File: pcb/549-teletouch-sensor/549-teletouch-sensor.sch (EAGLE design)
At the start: 87 parts, among them J1 RASPBERRYPI-40-PIN-GPIO_PTH, J2 RASPBERRYPI-40-PIN-GPIO_PTH

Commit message: updated sensor pcb
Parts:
- removed H1, H2, H3, H4: STAND-OFF, SparkFun-Hardware:STAND-OFF
- removed J2: RASPBERRYPI-40-PIN-GPIO_PTH, SparkFun-Connectors:RASPBERRYPI-40-PIN-GPIO_PTH
- added IC1, IC2: MCP23017SP, adafruit:MCP23017SP
- added SENSOR_ENDS1, SENSOR_ENDS2: CONN_20X2, SparkFun-Connectors:CONN_20X2
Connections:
- removed net GP41: J1.GP26
- removed net GP42: J1.GP4
- removed net GP43: J1.GP17
- removed net GP44: J1.GP18#
- removed net GP45: J1.GP22
- removed net GP46: J1.GP23
- removed net GP47: J1.GP24
- removed net GP48: J1.GP25
- removed net GP49: J1.GP27
- removed net N$11: R10.2
- removed net N$12: R1.2
- removed net N$13: R2.2
- removed net N$14: R3.2
- removed net N$15: R4.2
- removed net N$16: R5.2
- removed net N$17: R6.2
- removed net N$18: R7.2
- removed net N$19: R8.2
- removed net N$20: R9.2
- removed net N$31: R20.2
- removed net N$32: R11.2
- removed net N$33: R12.2
- removed net N$34: R13.2
- removed net N$35: R14.2
- removed net N$36: R15.2
- removed net N$37: R16.2
- removed net N$38: R17.2
- removed net N$39: R18.2
- removed net N$40: R19.2
- removed net N$51: R30.2
- removed net N$52: R21.2
- removed net N$53: R22.2
- removed net N$54: R23.2
- removed net N$55: R24.2
- removed net N$56: R25.2
- removed net N$57: R26.2
- removed net N$58: R27.2
- removed net N$59: R28.2
- removed net N$60: R29.2
- removed net N$71: R40.2
- removed net N$72: R31.2
- removed net N$73: R32.2
- removed net N$74: R33.2
- removed net N$75: R34.2
- removed net N$76: R35.2
- removed net N$77: R36.2
- removed net N$78: R37.2
- removed net N$79: R38.2
- removed net N$80: R39.2
- new net S1: R10.2, SENSOR_ENDS1.1
- new net S10: R9.2, SENSOR_ENDS1.19
- new net S11: R20.2, SENSOR_ENDS1.21
- new net S12: R11.2, SENSOR_ENDS1.23
- new net S13: R12.2, SENSOR_ENDS1.25
- new net S14: R13.2, SENSOR_ENDS1.27
- new net S15: R14.2, SENSOR_ENDS1.29
- new net S16: R15.2, SENSOR_ENDS1.31
- new net S17: R16.2, SENSOR_ENDS1.33
- new net S18: R17.2, SENSOR_ENDS1.35
- new net S19: R18.2, SENSOR_ENDS1.37
- new net S2: R1.2, SENSOR_ENDS1.3
- new net S20: R19.2, SENSOR_ENDS1.39
- new net S21: R30.2, SENSOR_ENDS1.2
- new net S22: R21.2, SENSOR_ENDS1.4
- new net S23: R22.2, SENSOR_ENDS1.6
- new net S24: R23.2, SENSOR_ENDS1.8
- new net S25: R24.2, SENSOR_ENDS1.10
- new net S26: R25.2, SENSOR_ENDS1.12
- new net S27: R26.2, SENSOR_ENDS1.14
- new net S28: R27.2, SENSOR_ENDS1.16
- new net S29: R28.2, SENSOR_ENDS1.18
- new net S3: R2.2, SENSOR_ENDS1.5
- new net S30: R29.2, SENSOR_ENDS1.20
- new net S31: R40.2, SENSOR_ENDS1.22
- new net S32: R31.2, SENSOR_ENDS1.24
- new net S33: R32.2, SENSOR_ENDS1.26
- new net S34: R33.2, SENSOR_ENDS1.28
- new net S35: R34.2, SENSOR_ENDS1.30
- new net S36: R35.2, SENSOR_ENDS1.32
- new net S37: R36.2, SENSOR_ENDS1.34
- new net S38: R37.2, SENSOR_ENDS1.36
- new net S39: R38.2, SENSOR_ENDS1.38
- new net S4: R3.2, SENSOR_ENDS1.7
- new net S40: R39.2, SENSOR_ENDS1.40
- new net S5: R4.2, SENSOR_ENDS1.9
- new net S6: R5.2, SENSOR_ENDS1.11
- new net S7: R6.2, SENSOR_ENDS1.13
- new net S8: R7.2, SENSOR_ENDS1.15
- new net S9: R8.2, SENSOR_ENDS1.17
- net GND: now also IC1.A0, IC1.A1, IC1.A2, IC1.VSS, IC2.A1, IC2.A2, IC2.VSS
- net GP1: now also IC2.GPA0, SENSOR_ENDS2.1; no longer J2.TXO
- net GP10: now also IC2.GPB1, SENSOR_ENDS2.19; no longer J2.GP18#
- net GP11: now also IC2.GPB2, SENSOR_ENDS2.21; no longer J2.GP22
- net GP12: now also IC2.GPB3, SENSOR_ENDS2.23; no longer J2.GP23
- net GP13: now also IC2.GPB4, SENSOR_ENDS2.25; no longer J2.GP24
- net GP14: now also IC2.GPB5, SENSOR_ENDS2.27; no longer J2.GP25
- net GP15: now also IC2.GPB6, SENSOR_ENDS2.29; no longer J2.GP27
- net GP16: now also IC2.GPB7, SENSOR_ENDS2.31; no longer J2.ID_SD
- net GP17: now also IC1.GPA0, SENSOR_ENDS2.33; no longer J2.ID_SC
- net GP18: now also IC1.GPA1, SENSOR_ENDS2.35; no longer J2.5V@2
- net GP19: now also IC1.GPA2, SENSOR_ENDS2.37; no longer J2.5V@4
- net GP2: now also IC2.GPA1, SENSOR_ENDS2.3; no longer J2.RXI
- net GP20: now also IC1.GPA3, SENSOR_ENDS2.39; no longer J2.3.3V@1
- net GP21: now also IC1.GPA4, SENSOR_ENDS2.2; no longer J2.3.3V@17
- net GP22: now also IC1.GPA5, SENSOR_ENDS2.4; no longer J2.GP5
- net GP23: now also IC1.GPA6, SENSOR_ENDS2.6; no longer J2.GP6
- net GP24: now also IC1.GPA7, SENSOR_ENDS2.8; no longer J2.GP12
- net GP25: now also IC1.GPB0, SENSOR_ENDS2.10; no longer J2.GP13
- net GP26: now also IC1.GPB1, SENSOR_ENDS2.12; no longer J2.GP16
- net GP27: now also IC1.GPB2, SENSOR_ENDS2.14; no longer J2.GP19
- net GP28: now also IC1.GPB3, SENSOR_ENDS2.16; no longer J2.GP20
- net GP29: now also IC1.GPB4, SENSOR_ENDS2.18; no longer J2.GP21
- net GP3: now also IC2.GPA2, SENSOR_ENDS2.5; no longer J2.SCLK
- net GP30: now also IC1.GPB5, SENSOR_ENDS2.20; no longer J2.GP26
- net GP31: now also IC1.GPB6, SENSOR_ENDS2.22; no longer J2.GND@6
- net GP32: now also IC1.GPB7, SENSOR_ENDS2.24; no longer J2.GND@9
- net GP33: now also SENSOR_ENDS2.26; no longer J2.GND@14
- net GP34: now also SENSOR_ENDS2.28; no longer J2.GND@20
- net GP35: now also SENSOR_ENDS2.30; no longer J2.GND@25
- net GP36: now also SENSOR_ENDS2.32; no longer J2.GND@30
- net GP37: now also SENSOR_ENDS2.34; no longer J2.GND@34
- net GP38: now also SENSOR_ENDS2.36; no longer J2.GND@39
- net GP39: now also SENSOR_ENDS2.38; no longer J2.SDA
- net GP4: now also IC2.GPA3, SENSOR_ENDS2.7; no longer J2.MISO
- net GP40: now also SENSOR_ENDS2.40; no longer J2.SCL
- net GP5: now also IC2.GPA4, SENSOR_ENDS2.9; no longer J2.MOSI
- net GP6: now also IC2.GPA5, SENSOR_ENDS2.11; no longer J2.CE0
- net GP7: now also IC2.GPA6, SENSOR_ENDS2.13; no longer J2.CE1
- net GP8: now also IC2.GPA7, SENSOR_ENDS2.15; no longer J2.GP4
- net GP9: now also IC2.GPB0, SENSOR_ENDS2.17; no longer J2.GP17
- net SCL: now also IC1.SCL, IC2.SCL
- net SDA: now also IC1.SDA, IC2.SDA
- net VDD: now also IC1.!RESET, IC1.VDD, IC2.!RESET, IC2.A0, IC2.VDD
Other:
- moved on the sheet: C1, C10, C11, C12, C13, C14, C15, C16, C17, C18, C19, C2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

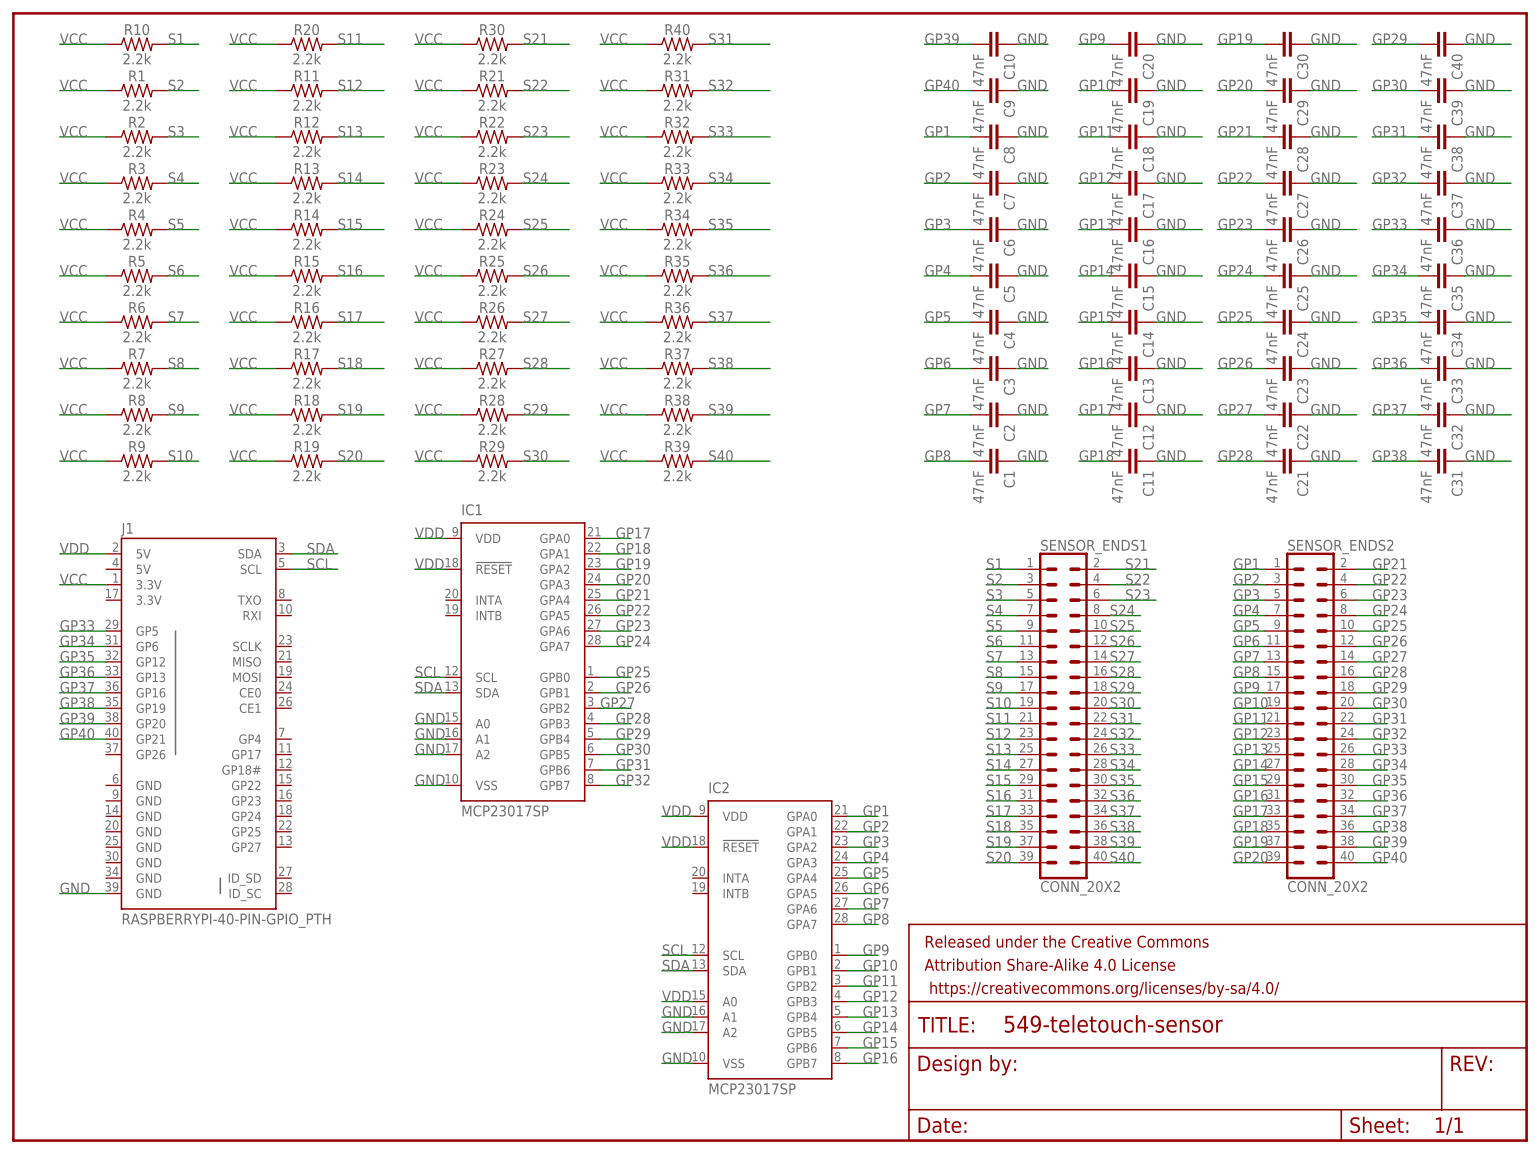
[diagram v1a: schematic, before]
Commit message: updated to half the amount of sensors
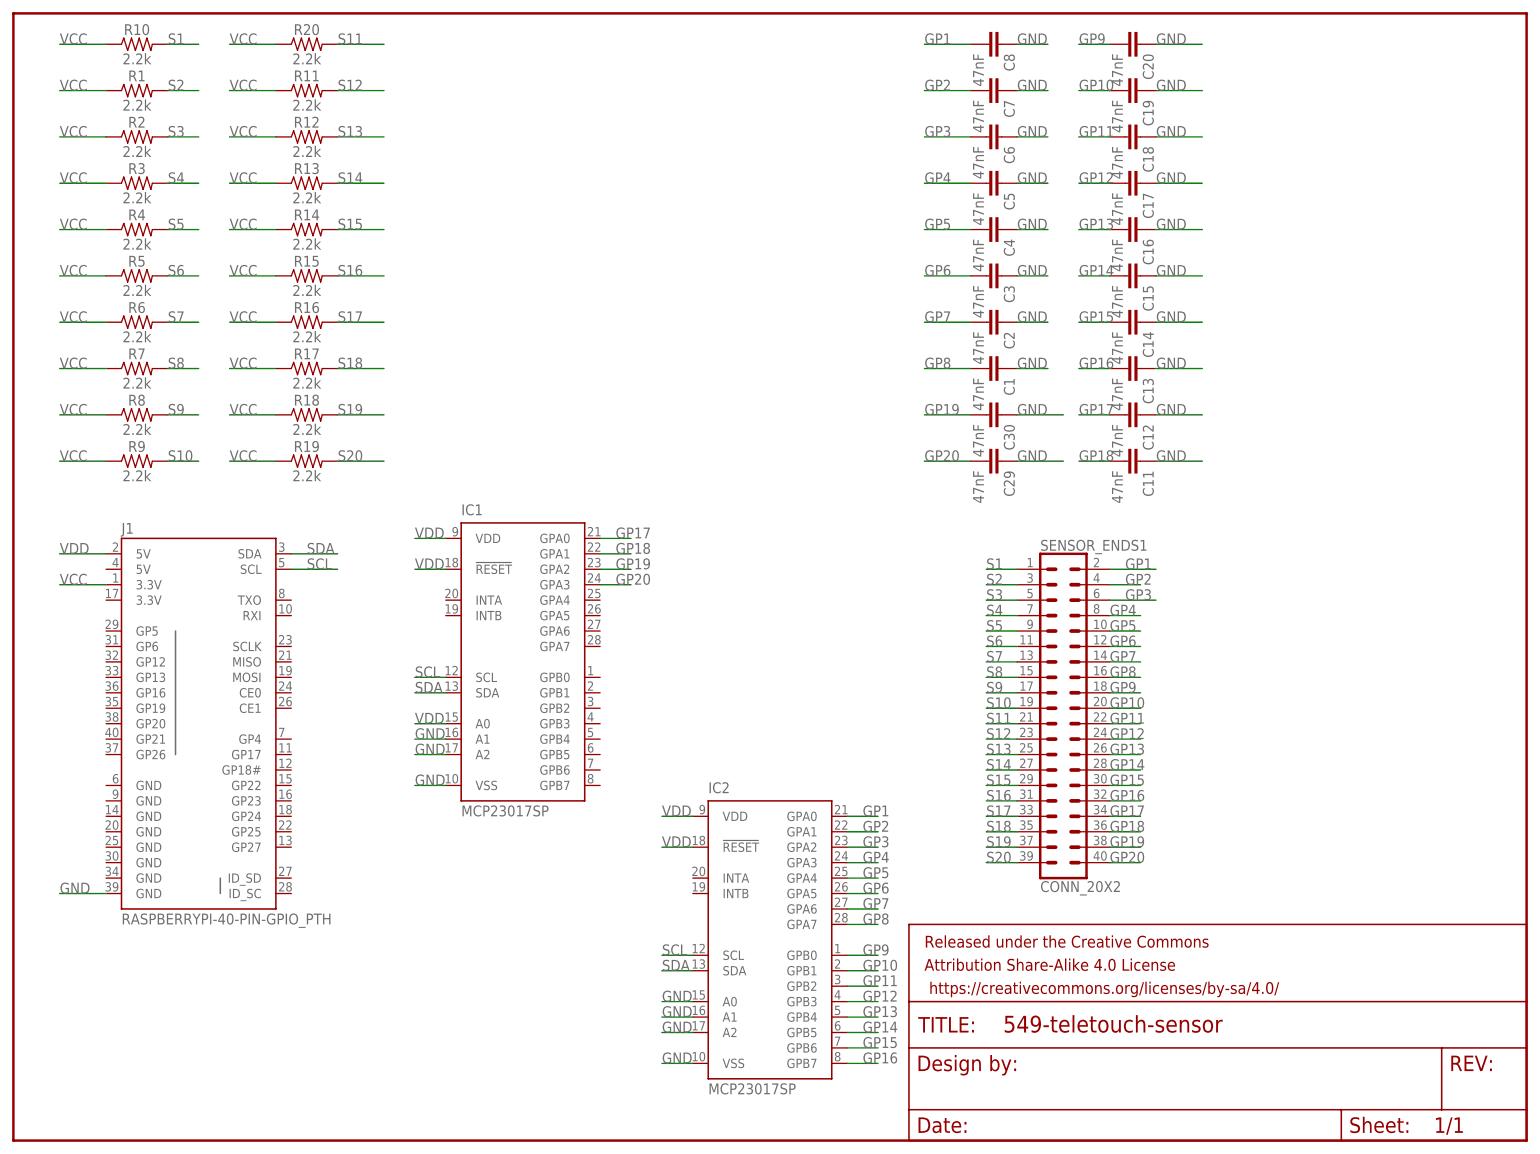
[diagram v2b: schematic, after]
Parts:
- removed C10, C21, C22, C23, C24, C25, C26, C27, C28, C31, C32, C33, C34, C35, C36, C37, C38, C39, C40, C9: 47nF, SparkFun-Capacitors:47NF-0603-25V-5%
- removed R21, R22, R23, R24, R25, R26, R27, R28, R29, R30, R31, R32, R33, R34, R35, R36, R37, R38, R39, R40: 2.2k, SparkFun-Resistors:2.2KOHM-0603-1/10W-1%
- removed SENSOR_ENDS2: CONN_20X2, SparkFun-Connectors:CONN_20X2
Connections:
- removed net GP21: C28.2, IC1.GPA4, SENSOR_ENDS2.2
- removed net GP22: C27.2, IC1.GPA5, SENSOR_ENDS2.4
- removed net GP23: C26.2, IC1.GPA6, SENSOR_ENDS2.6
- removed net GP24: C25.2, IC1.GPA7, SENSOR_ENDS2.8
- removed net GP25: C24.2, IC1.GPB0, SENSOR_ENDS2.10
- removed net GP26: C23.2, IC1.GPB1, SENSOR_ENDS2.12
- removed net GP27: C22.2, IC1.GPB2, SENSOR_ENDS2.14
- removed net GP28: C21.2, IC1.GPB3, SENSOR_ENDS2.16
- removed net GP29: C40.2, IC1.GPB4, SENSOR_ENDS2.18
- removed net GP30: C39.2, IC1.GPB5, SENSOR_ENDS2.20
- removed net GP31: C38.2, IC1.GPB6, SENSOR_ENDS2.22
- removed net GP32: C37.2, IC1.GPB7, SENSOR_ENDS2.24
- removed net GP33: C36.2, J1.GP5, SENSOR_ENDS2.26
- removed net GP34: C35.2, J1.GP6, SENSOR_ENDS2.28
- removed net GP35: C34.2, J1.GP12, SENSOR_ENDS2.30
- removed net GP36: C33.2, J1.GP13, SENSOR_ENDS2.32
- removed net GP37: C32.2, J1.GP16, SENSOR_ENDS2.34
- removed net GP38: C31.2, J1.GP19, SENSOR_ENDS2.36
- removed net GP39: C10.2, J1.GP20, SENSOR_ENDS2.38
- removed net GP40: C9.2, J1.GP21, SENSOR_ENDS2.40
- removed net S21: R30.2, SENSOR_ENDS1.2
- removed net S22: R21.2, SENSOR_ENDS1.4
- removed net S23: R22.2, SENSOR_ENDS1.6
- removed net S24: R23.2, SENSOR_ENDS1.8
- removed net S25: R24.2, SENSOR_ENDS1.10
- removed net S26: R25.2, SENSOR_ENDS1.12
- removed net S27: R26.2, SENSOR_ENDS1.14
- removed net S28: R27.2, SENSOR_ENDS1.16
- removed net S29: R28.2, SENSOR_ENDS1.18
- removed net S30: R29.2, SENSOR_ENDS1.20
- removed net S31: R40.2, SENSOR_ENDS1.22
- removed net S32: R31.2, SENSOR_ENDS1.24
- removed net S33: R32.2, SENSOR_ENDS1.26
- removed net S34: R33.2, SENSOR_ENDS1.28
- removed net S35: R34.2, SENSOR_ENDS1.30
- removed net S36: R35.2, SENSOR_ENDS1.32
- removed net S37: R36.2, SENSOR_ENDS1.34
- removed net S38: R37.2, SENSOR_ENDS1.36
- removed net S39: R38.2, SENSOR_ENDS1.38
- removed net S40: R39.2, SENSOR_ENDS1.40
- net GND: now also IC2.A0; no longer C10.1, C21.1, C22.1, C23.1, C24.1, C25.1, C26.1, C27.1, C28.1, C31.1, C32.1, C33.1, C34.1, C35.1, C36.1, C37.1, C38.1, C39.1, C40.1, C9.1, IC1.A0
- net GP1: now also SENSOR_ENDS1.2; no longer SENSOR_ENDS2.1
- net GP10: now also SENSOR_ENDS1.20; no longer SENSOR_ENDS2.19
- net GP11: now also SENSOR_ENDS1.22; no longer SENSOR_ENDS2.21
- net GP12: now also SENSOR_ENDS1.24; no longer SENSOR_ENDS2.23
- net GP13: now also SENSOR_ENDS1.26; no longer SENSOR_ENDS2.25
- net GP14: now also SENSOR_ENDS1.28; no longer SENSOR_ENDS2.27
- net GP15: now also SENSOR_ENDS1.30; no longer SENSOR_ENDS2.29
- net GP16: now also SENSOR_ENDS1.32; no longer SENSOR_ENDS2.31
- net GP17: now also SENSOR_ENDS1.34; no longer SENSOR_ENDS2.33
- net GP18: now also SENSOR_ENDS1.36; no longer SENSOR_ENDS2.35
- net GP19: now also SENSOR_ENDS1.38; no longer SENSOR_ENDS2.37
- net GP2: now also SENSOR_ENDS1.4; no longer SENSOR_ENDS2.3
- net GP20: now also SENSOR_ENDS1.40; no longer SENSOR_ENDS2.39
- net GP3: now also SENSOR_ENDS1.6; no longer SENSOR_ENDS2.5
- net GP4: now also SENSOR_ENDS1.8; no longer SENSOR_ENDS2.7
- net GP5: now also SENSOR_ENDS1.10; no longer SENSOR_ENDS2.9
- net GP6: now also SENSOR_ENDS1.12; no longer SENSOR_ENDS2.11
- net GP7: now also SENSOR_ENDS1.14; no longer SENSOR_ENDS2.13
- net GP8: now also SENSOR_ENDS1.16; no longer SENSOR_ENDS2.15
- net GP9: now also SENSOR_ENDS1.18; no longer SENSOR_ENDS2.17
- net VCC: no longer R21.1, R22.1, R23.1, R24.1, R25.1, R26.1, R27.1, R28.1, R29.1, R30.1, R31.1, R32.1, R33.1, R34.1, R35.1, R36.1, R37.1, R38.1, R39.1, R40.1
- net VDD: now also IC1.A0; no longer IC2.A0
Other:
- moved on the sheet: C1, C2, C29, C3, C30, C4, C5, C6, C7, C8
